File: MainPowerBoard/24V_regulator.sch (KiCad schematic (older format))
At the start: 17 parts, among them U201 LMR16030S

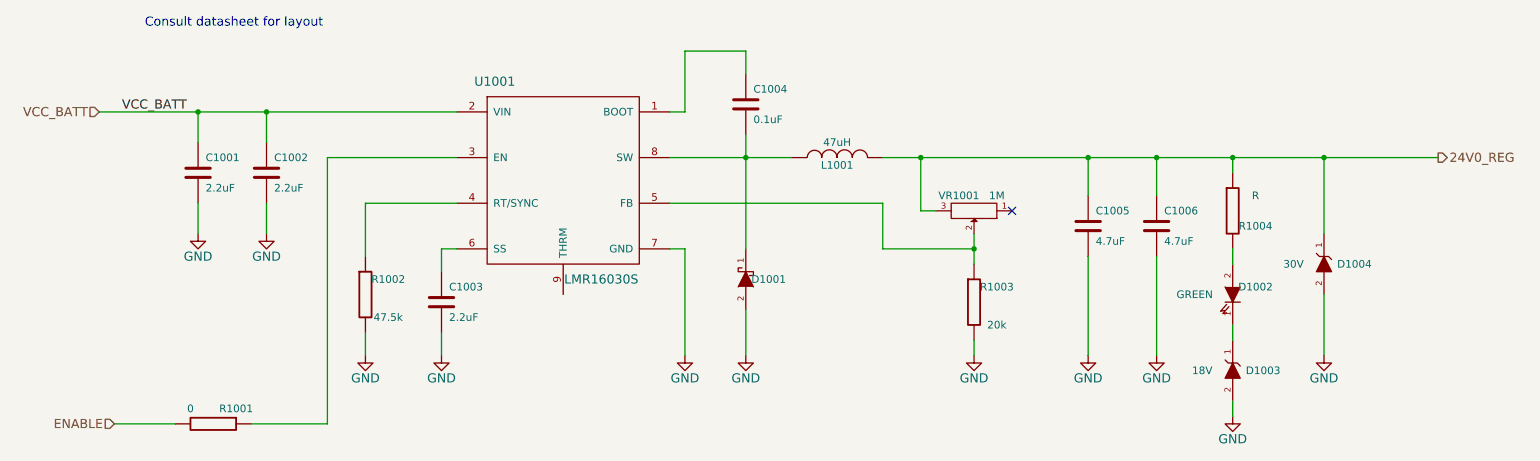
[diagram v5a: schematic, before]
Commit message: Continued layout of MainPowerBoard
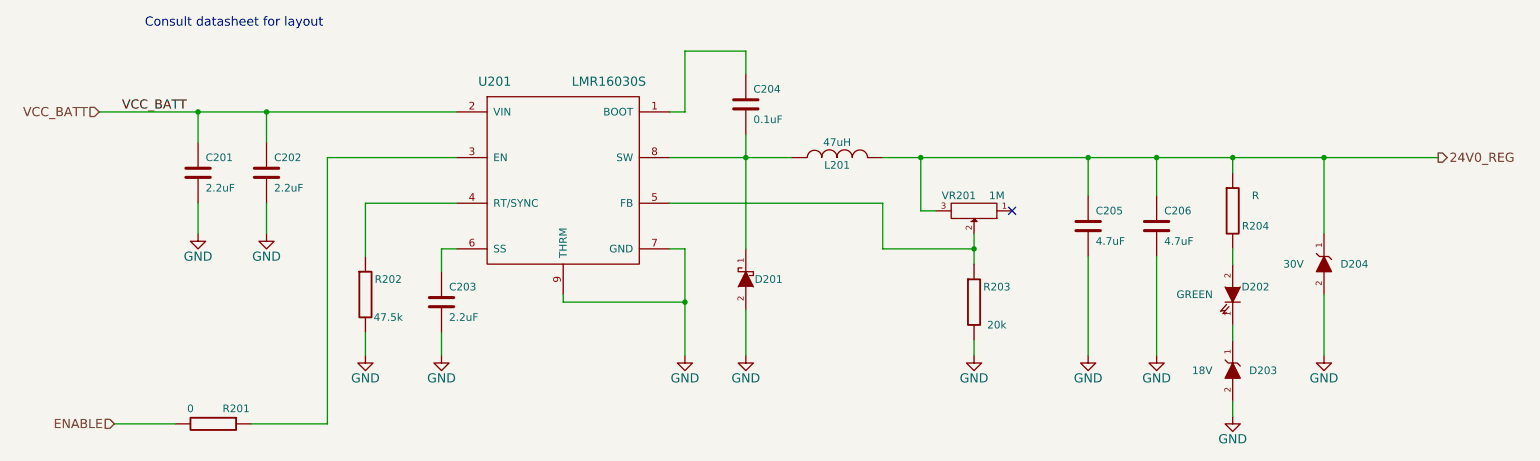
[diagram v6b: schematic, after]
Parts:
- D203: footprint Diodes_SMD:SMB_Handsoldering -> Diodes_SMD:SMA_Handsoldering; DigiKey PN 1SMB5931B-13DICT-ND -> 1SMA5931BT3GOSCT-ND; Mfg. Diodes -> ON Semi; Mfg. PN 1SMB5931B-13 -> 1SMA5931BT3G
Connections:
- net GND: now also U201.9 (THRM)
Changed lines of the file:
@@
 AR Path="/583A9416/5833A728" Ref="R1304"  Part="1"
 AR Path="/583A941B/5833A728" Ref="R1404"  Part="1"
-F 0 "R1004" H 8750 3950 50  0000 C CNN
+F 0 "R204" H 8750 3950 50  0000 C CNN
 F 1 "R" H 8750 4150 50  0000 C CNN
 F 2 "Resistors_SMD:R_1206_HandSoldering" V 8530 4050 30  0001 C CNN
@@
 AR Path="/583A9416/583A8678" Ref="U1301"  Part="1"
 AR Path="/583A941B/583A8678" Ref="U1401"  Part="1"
-F 0 "U1001" H 3750 4500 60  0000 C CNN
-F 1 "LMR16030S" H 4450 3200 60  0000 C CNN
+F 0 "U201" H 3750 4500 60  0000 C CNN
+F 1 "LMR16030S" H 4500 4500 60  0000 C CNN
 F 2 "hyperCustom:LMR16030S_8-PowerSOIC_TI" H 4150 3850 60  0001 C CNN
 F 3 "" H 4150 3850 60  0000 C CNN
@@
 AR Path="/583A9416/583A8A9A" Ref="C1301"  Part="1"
 AR Path="/583A941B/583A8A9A" Ref="C1401"  Part="1"
-F 0 "C1001" H 1850 3900 50  0000 L CNN
+F 0 "C201" H 1850 3900 50  0000 L CNN
 F 1 "2.2uF" H 1850 3700 50  0000 L CNN
 F 2 "Capacitors_SMD:C_1210_HandSoldering" H 1838 3650 30  0001 C CNN
@@
 AR Path="/583A9416/583A8B4B" Ref="C1302"  Part="1"
 AR Path="/583A941B/583A8B4B" Ref="C1402"  Part="1"
-F 0 "C1002" H 2300 3900 50  0000 L CNN
+F 0 "C202" H 2300 3900 50  0000 L CNN
 F 1 "2.2uF" H 2300 3700 50  0000 L CNN
 F 2 "Capacitors_SMD:C_1210_HandSoldering" H 2288 3650 30  0001 C CNN
@@
 AR Path="/583A9416/583A8BF8" Ref="#PWR0100"  Part="1"
 AR Path="/583A941B/583A8BF8" Ref="#PWR0111"  Part="1"
-F 0 "#PWR0111" H 1800 3950 60  0001 C CNN
+F 0 "#PWR016" H 1800 3950 60  0001 C CNN
 F 1 "GND" H 1800 4050 60  0000 C CNN
 F 2 "" H 1800 4200 60  0000 C CNN
@@
 AR Path="/583A9416/583A8C28" Ref="#PWR0101"  Part="1"
 AR Path="/583A941B/583A8C28" Ref="#PWR0112"  Part="1"
-F 0 "#PWR0112" H 2250 3950 60  0001 C CNN
+F 0 "#PWR017" H 2250 3950 60  0001 C CNN
 F 1 "GND" H 2250 4050 60  0000 C CNN
 F 2 "" H 2250 4200 60  0000 C CNN
@@
 AR Path="/583A9416/583A8CF1" Ref="C1303"  Part="1"
 AR Path="/583A941B/583A8CF1" Ref="C1403"  Part="1"
-F 0 "C1003" H 3450 4750 50  0000 L CNN
+F 0 "C203" H 3450 4750 50  0000 L CNN
 F 1 "2.2uF" H 3450 4550 50  0000 L CNN
 F 2 "Resistors_SMD:R_0805_HandSoldering" H 3438 4500 30  0001 C CNN
@@
 AR Path="/583A9416/583A8E72" Ref="#PWR0102"  Part="1"
 AR Path="/583A941B/583A8E72" Ref="#PWR0113"  Part="1"
-F 0 "#PWR0113" H 2900 4750 60  0001 C CNN
+F 0 "#PWR018" H 2900 4750 60  0001 C CNN
 F 1 "GND" H 2900 4850 60  0000 C CNN
 F 2 "" H 2900 5000 60  0000 C CNN
@@
 AR Path="/583A9416/583A8EBE" Ref="#PWR0103"  Part="1"
 AR Path="/583A941B/583A8EBE" Ref="#PWR0114"  Part="1"
-F 0 "#PWR0114" H 3400 4750 60  0001 C CNN
+F 0 "#PWR019" H 3400 4750 60  0001 C CNN
 F 1 "GND" H 3400 4850 60  0000 C CNN
 F 2 "" H 3400 5000 60  0000 C CNN
@@
 AR Path="/583A9416/583B27BB" Ref="#PWR0104"  Part="1"
 AR Path="/583A941B/583B27BB" Ref="#PWR0115"  Part="1"
-F 0 "#PWR0115" H 5000 4750 60  0001 C CNN
+F 0 "#PWR020" H 5000 4750 60  0001 C CNN
 F 1 "GND" H 5000 4850 60  0000 C CNN
 F 2 "" H 5000 5000 60  0000 C CNN
@@
 AR Path="/583A9416/583B2967" Ref="R1303"  Part="1"
 AR Path="/583A941B/583B2967" Ref="R1403"  Part="1"
-F 0 "R1003" H 7050 4750 50  0000 C CNN
+F 0 "R203" H 7050 4750 50  0000 C CNN
 F 1 "20k" H 7050 4500 50  0000 C CNN
 F 2 "Resistors_SMD:R_1206_HandSoldering" V 6830 4650 30  0001 C CNN
@@
 AR Path="/583A9416/583B2A2E" Ref="VR1301"  Part="1"
 AR Path="/583A941B/583B2A2E" Ref="VR1401"  Part="1"
-F 0 "VR1001" H 7000 3950 50  0000 C CNN
+F 0 "VR201" H 7000 3950 50  0000 C CNN
 F 1 "1M" H 6750 3950 50  0000 C CNN
 F 2 "hyperCustom:BOURNS_MULTITURNPOT_3299W" H 6900 4050 60  0001 C CNN
@@
 AR Path="/583A9416/583B2BCB" Ref="D1301"  Part="1"
 AR Path="/583A941B/583B2BCB" Ref="D1401"  Part="1"
-F 0 "D1001" V 5400 4350 50  0000 C CNN
+F 0 "D201" V 5400 4350 50  0000 C CNN
 F 1 "DIODESCH" H 5400 4400 50  0001 C CNN
 F 2 "Diodes_SMD:SMA_Handsoldering" H 5400 4500 60  0001 C CNN
@@
 AR Path="/583A9416/583B2C66" Ref="#PWR0105"  Part="1"
 AR Path="/583A941B/583B2C66" Ref="#PWR0116"  Part="1"
-F 0 "#PWR0116" H 5400 4750 60  0001 C CNN
+F 0 "#PWR021" H 5400 4750 60  0001 C CNN
 F 1 "GND" H 5400 4850 60  0000 C CNN
 F 2 "" H 5400 5000 60  0000 C CNN
@@
 AR Path="/583A9416/583B2D59" Ref="L1301"  Part="1"
 AR Path="/583A941B/583B2D59" Ref="L1401"  Part="1"
-F 0 "L1001" V 5950 3700 50  0000 C CNN
+F 0 "L201" V 5950 3700 50  0000 C CNN
 F 1 "47uH" V 6100 3700 50  0000 C CNN
 F 2 "hyperCustom:47uIND_CDRH127_LDNP-470MC_SUMIDA" H 6000 3700 60  0001 C CNN
@@
 AR Path="/583A9416/583B307C" Ref="#PWR0106"  Part="1"
 AR Path="/583A941B/583B307C" Ref="#PWR0117"  Part="1"
-F 0 "#PWR0117" H 6900 4750 60  0001 C CNN
+F 0 "#PWR022" H 6900 4750 60  0001 C CNN
 F 1 "GND" H 6900 4850 60  0000 C CNN
 F 2 "" H 6900 5000 60  0000 C CNN
@@
 AR Path="/583A9416/583B399E" Ref="C1304"  Part="1"
 AR Path="/583A941B/583B399E" Ref="C1404"  Part="1"
-F 0 "C1004" H 5450 3450 50  0000 L CNN
+F 0 "C204" H 5450 3450 50  0000 L CNN
 F 1 "0.1uF" H 5450 3250 50  0000 L CNN
 F 2 "Resistors_SMD:R_1206_HandSoldering" H 5438 3200 30  0001 C CNN
@@
 AR Path="/583A9416/583B4188" Ref="C1305"  Part="1"
 AR Path="/583A941B/583B4188" Ref="C1405"  Part="1"
-F 0 "C1005" H 7700 4250 50  0000 L CNN
+F 0 "C205" H 7700 4250 50  0000 L CNN
 F 1 "4.7uF" H 7700 4050 50  0000 L CNN
 F 2 "Capacitors_SMD:C_1206_HandSoldering" H 7688 4000 30  0001 C CNN
@@
 AR Path="/583A9416/583B42A9" Ref="#PWR0107"  Part="1"
 AR Path="/583A941B/583B42A9" Ref="#PWR0118"  Part="1"
-F 0 "#PWR0118" H 7650 4750 60  0001 C CNN
+F 0 "#PWR023" H 7650 4750 60  0001 C CNN
 F 1 "GND" H 7650 4850 60  0000 C CNN
 F 2 "" H 7650 5000 60  0000 C CNN
@@
 AR Path="/583A9416/583B43AD" Ref="C1306"  Part="1"
 AR Path="/583A941B/583B43AD" Ref="C1406"  Part="1"
-F 0 "C1006" H 8150 4250 50  0000 L CNN
+F 0 "C206" H 8150 4250 50  0000 L CNN
 F 1 "4.7uF" H 8150 4050 50  0000 L CNN
 F 2 "Capacitors_SMD:C_1206_HandSoldering" H 8138 4000 30  0001 C CNN
@@
 AR Path="/583A9416/583B449E" Ref="#PWR0108"  Part="1"
 AR Path="/583A941B/583B449E" Ref="#PWR0119"  Part="1"
-F 0 "#PWR0119" H 8100 4750 60  0001 C CNN
+F 0 "#PWR024" H 8100 4750 60  0001 C CNN
 F 1 "GND" H 8100 4850 60  0000 C CNN
 F 2 "" H 8100 5000 60  0000 C CNN
@@
 AR Path="/583A9416/583D36BC" Ref="R1301"  Part="1"
 AR Path="/583A941B/583D36BC" Ref="R1401"  Part="1"
-F 0 "R1001" V 1800 5600 50  0000 C CNN
+F 0 "R201" V 1800 5600 50  0000 C CNN
 F 1 "0" V 1800 5300 50  0000 C CNN
 F 2 "Resistors_SMD:R_1206_HandSoldering" V 1830 5450 30  0001 C CNN
@@
 AR Path="/583A9416/583D8D48" Ref="D1303"  Part="1"
 AR Path="/583A941B/583D8D48" Ref="D1403"  Part="1"
-F 0 "D1003" V 8600 4900 50  0000 C CNN
+F 0 "D203" V 8600 4900 50  0000 C CNN
 F 1 "18V" V 8600 5300 50  0000 C CNN
-F 2 "Diodes_SMD:SMB_Handsoldering" H 8600 5100 60  0001 C CNN
+F 2 "Diodes_SMD:SMA_Handsoldering" H 8600 5100 60  0001 C CNN
 F 3 "" H 8600 5100 60  0000 C CNN
-F 4 "Diodes" V 8600 5100 60  0001 C CNN "Mfg."
-F 5 "1SMB5931B-13" V 8600 5100 60  0001 C CNN "Mfg. PN"
-F 6 "1SMB5931B-13DICT-ND" V 8600 5100 60  0001 C CNN "DigiKey PN"
+F 4 "ON Semi" V 8600 5100 60  0001 C CNN "Mfg."
+F 5 "1SMA5931BT3G" V 8600 5100 60  0001 C CNN "Mfg. PN"
+F 6 "1SMA5931BT3GOSCT-ND" V 8600 5100 60  0001 C CNN "DigiKey PN"
 	1    8600 5100
 	0    -1   -1   0
@@
 AR Path="/583A9416/583D8F40" Ref="#PWR0109"  Part="1"
 AR Path="/583A941B/583D8F40" Ref="#PWR0120"  Part="1"
-F 0 "#PWR0120" H 8600 5150 60  0001 C CNN
+F 0 "#PWR025" H 8600 5150 60  0001 C CNN
 F 1 "GND" H 8600 5250 60  0000 C CNN
 F 2 "" H 8600 5400 60  0000 C CNN
@@
 AR Path="/583A9416/583D986C" Ref="D1304"  Part="1"
 AR Path="/583A941B/583D986C" Ref="D1404"  Part="1"
-F 0 "D1004" V 9200 4200 50  0000 C CNN
+F 0 "D204" V 9200 4200 50  0000 C CNN
 F 1 "30V" V 9200 4600 50  0000 C CNN
 F 2 "Diodes_SMD:SMB_Handsoldering" H 9200 4400 60  0001 C CNN
@@
 AR Path="/583A9416/583D98F6" Ref="#PWR0110"  Part="1"
 AR Path="/583A941B/583D98F6" Ref="#PWR0121"  Part="1"
-F 0 "#PWR0121" H 9200 4750 60  0001 C CNN
+F 0 "#PWR026" H 9200 4750 60  0001 C CNN
 F 1 "GND" H 9200 4850 60  0000 C CNN
 F 2 "" H 9200 5000 60  0000 C CNN
@@
 AR Path="/583A9416/583E258D" Ref="R1302"  Part="1"
 AR Path="/583A941B/583E258D" Ref="R1402"  Part="1"
-F 0 "R1002" H 3050 4700 50  0000 C CNN
+F 0 "R202" H 3050 4700 50  0000 C CNN
 F 1 "47.5k" H 3050 4450 50  0000 C CNN
 F 2 "Resistors_SMD:R_1206_HandSoldering" V 2830 4600 30  0001 C CNN
@@
 AR Path="/583A9416/583D0112" Ref="D1302"  Part="1"
 AR Path="/583A941B/583D0112" Ref="D1402"  Part="1"
-F 0 "D1002" V 8550 4750 50  0000 C CNN
+F 0 "D202" V 8550 4750 50  0000 C CNN
 F 1 "GREEN" V 8600 4350 50  0000 C CNN
 F 2 "LEDs:LED_1206" H 8600 4600 60  0001 C CNN
@@
 	0    1    1    0
 $EndComp
+Wire Wire Line
+	4200 4600 4200 4650
+Wire Wire Line
+	4200 4650 5000 4650
+Connection ~ 5000 4650
 $EndSCHEMATC

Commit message: Continued working on layout. Fixed LED indicators for ON/OFF controller.
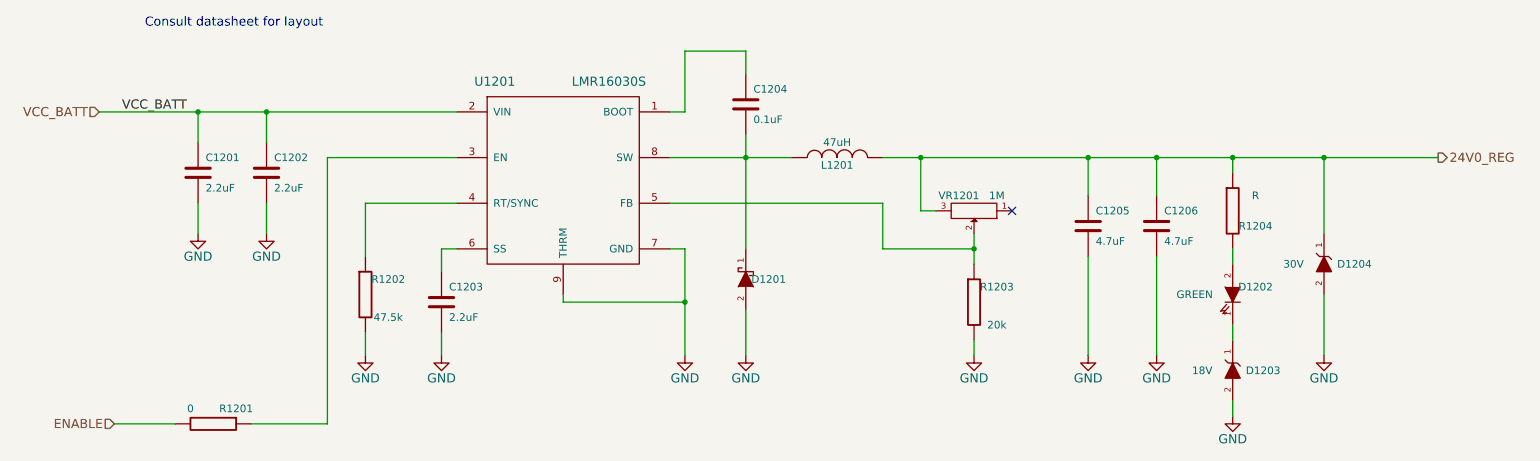
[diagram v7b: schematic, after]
